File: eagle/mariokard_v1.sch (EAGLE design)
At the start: 64 parts, among them SW1 KMR2, SW2 KMR2, U1 SPX3819, U3 ATMEGA32U4, U4 L298, X1 ESP-12, Y1 16MHz

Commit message: small fixes - still WIP
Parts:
- added U$29: FTDI_POGO, digikey:FTDI_POGO
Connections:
- removed net D5: U3.PC6
- removed net D6: U3.PD7(ADC10)
- removed net DIRA: U4.IN1, U4.IN2
- removed net DIRB: U4.IN3, U4.IN4
- removed net PWMA: U4.ENA
- removed net PWMB: U4.ENB
- new net DIRA1: U4.IN1
- new net DIRA2: U4.IN2
- new net DIRB1: U4.IN3
- new net DIRB2: U4.IN4
- new net PWMA/D5: U3.PC6, U4.ENA
- new net PWMB/D6: U3.PD7(ADC10), U4.ENB
- net GND: now also U$29.GND
- net RXD_5V: now also U$29.TXD
- net TXD: now also U$29.RXD
- net VIN: now also U$29.VCC
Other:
- note added: "3.3 Logic Voltage"
- note added: "COLOR SENSOR"
- note added: "connect things to ATMega"
- note removed: "3.3 Reg Voltage"
- note removed: "accelerometer"
- moved on the sheet: CN1, CN2, D1, D2, D21, D22, D23, D24, D3, D4, D5, D6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

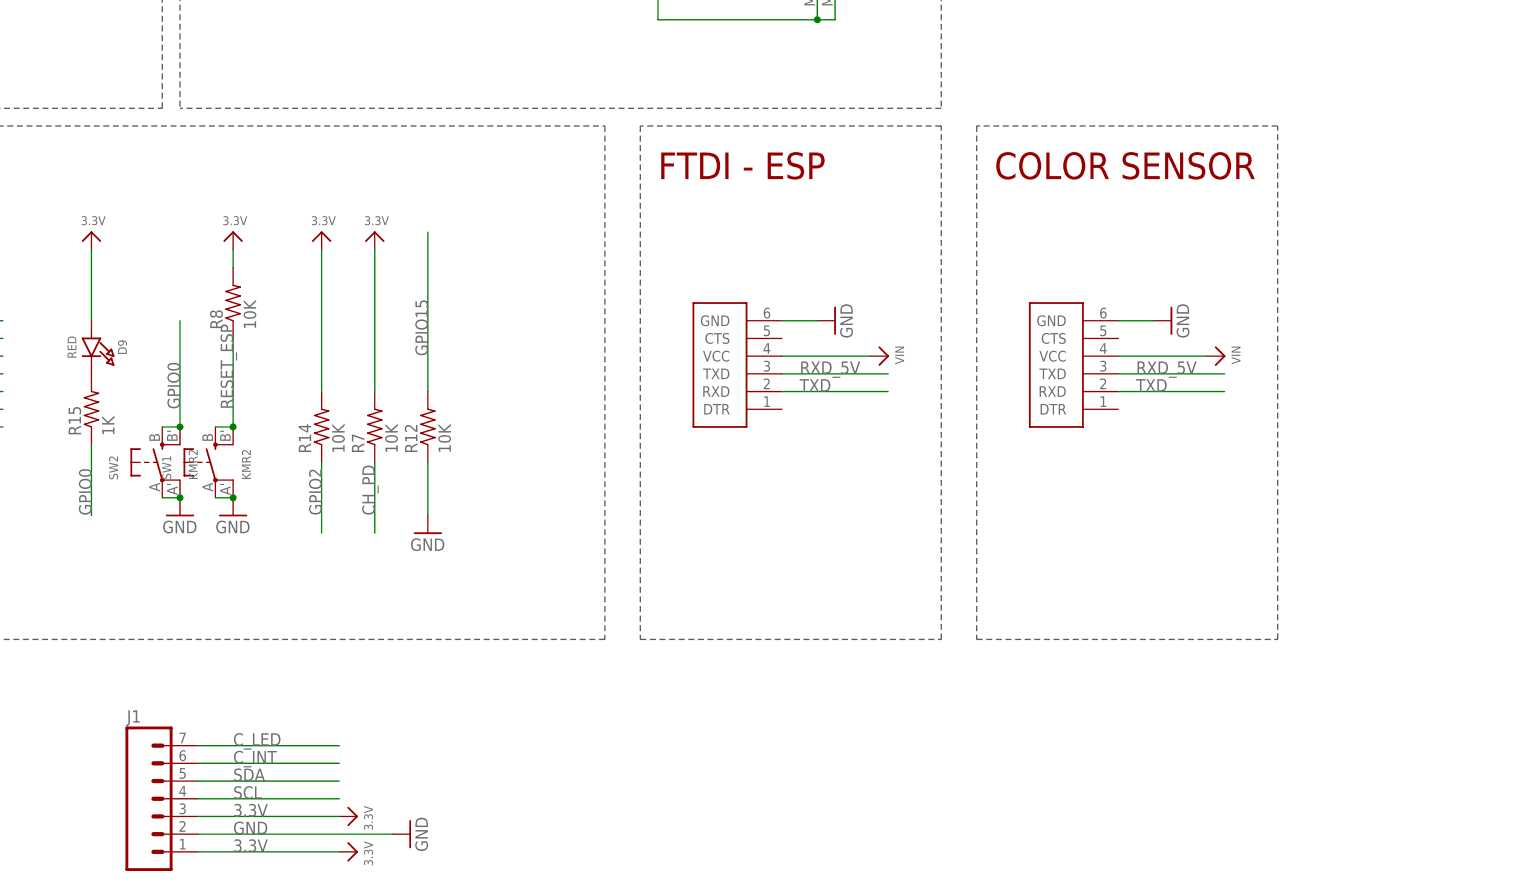
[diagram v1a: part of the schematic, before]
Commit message: fixed copy-paste error
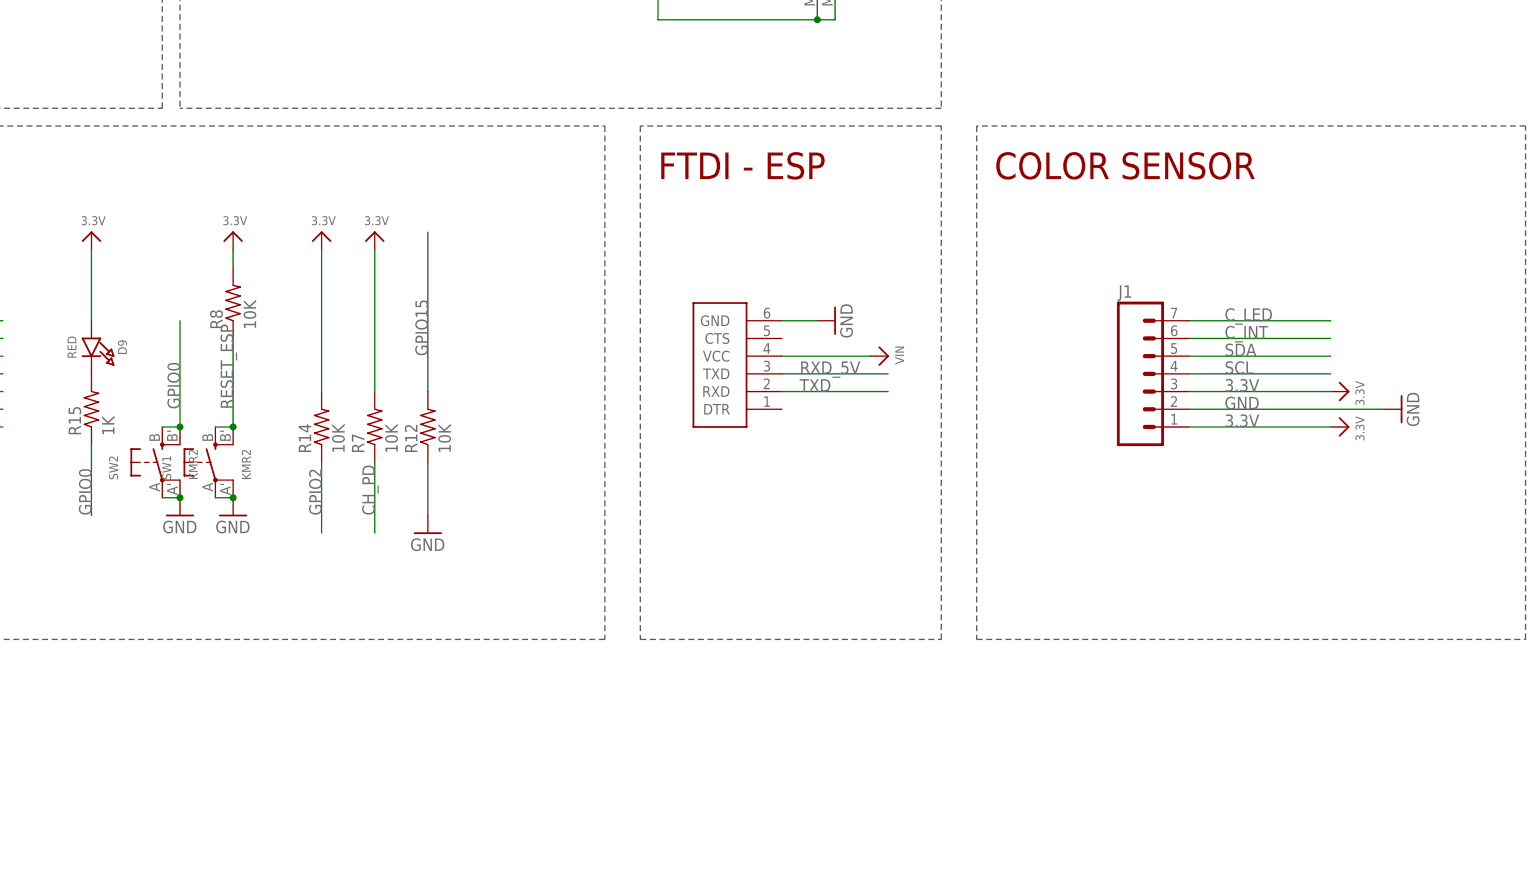
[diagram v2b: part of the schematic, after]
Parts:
- removed U$29: FTDI_POGO, digikey:FTDI_POGO
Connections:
- net GND: no longer U$29.GND
- net RXD_5V: no longer U$29.TXD
- net TXD: no longer U$29.RXD
- net VIN: no longer U$29.VCC
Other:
- moved on the sheet: J1
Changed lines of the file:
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@@
 <part name="GND15" library="supply1" deviceset="GND" device=""/>
 <part name="U$26" library="microbuilder" deviceset="3.3V" device=""/>
-<part name="U$29" library="digikey" deviceset="FTDI_POGO" device=""/>
-<part name="GND22" library="supply1" deviceset="GND" device=""/>
-<part name="U$35" library="microbuilder" deviceset="VIN" device=""/>
 </parts>
 <sheets>
@@
 <text x="22.86" y="-96.52" size="3.81" layer="94">Driver</text>
 <wire x1="411.48" y1="-35.56" x2="411.48" y2="-109.22" width="0.1524" layer="97" style="shortdash"/>
-<wire x1="411.48" y1="-109.22" x2="454.66" y2="-109.22" width="0.1524" layer="97" style="shortdash"/>
-<wire x1="454.66" y1="-109.22" x2="454.66" y2="-35.56" width="0.1524" layer="97" style="shortdash"/>
-<wire x1="454.66" y1="-35.56" x2="411.48" y2="-35.56" width="0.1524" layer="97" style="shortdash"/>
+<wire x1="411.48" y1="-109.22" x2="490.22" y2="-109.22" width="0.1524" layer="97" style="shortdash"/>
+<wire x1="490.22" y1="-109.22" x2="490.22" y2="-35.56" width="0.1524" layer="97" style="shortdash"/>
+<wire x1="490.22" y1="-35.56" x2="411.48" y2="-35.56" width="0.1524" layer="97" style="shortdash"/>
 <text x="414.02" y="-43.18" size="3.81" layer="94" ratio="10">COLOR SENSOR</text>
 <text x="-55.88" y="86.36" size="1.778" layer="97">connect things to ATMega</text>
@@
 <instance part="GND14" gate="1" x="241.3" y="60.96"/>
 <instance part="U$17" gate="G$1" x="165.1" y="86.36" rot="R90"/>
-<instance part="J1" gate="G$1" x="294.64" y="-134.62"/>
-<instance part="U$25" gate="G$1" x="322.58" y="-134.62" rot="R270"/>
-<instance part="GND15" gate="1" x="330.2" y="-137.16" rot="R90"/>
-<instance part="U$26" gate="G$1" x="322.58" y="-139.7" rot="R270"/>
-<instance part="U$29" gate="G$1" x="431.8" y="-63.5" rot="R180"/>
-<instance part="GND22" gate="1" x="439.42" y="-63.5" rot="R90"/>
-<instance part="U$35" gate="G$1" x="447.04" y="-68.58" rot="R270"/>
+<instance part="J1" gate="G$1" x="436.88" y="-73.66"/>
+<instance part="U$25" gate="G$1" x="464.82" y="-73.66" rot="R270"/>
+<instance part="GND15" gate="1" x="472.44" y="-76.2" rot="R90"/>
+<instance part="U$26" gate="G$1" x="464.82" y="-78.74" rot="R270"/>
 </instances>
 <busses>
@@
 <segment>
 <pinref part="J1" gate="G$1" pin="2"/>
-<wire x1="299.72" y1="-137.16" x2="327.66" y2="-137.16" width="0.1524" layer="91"/>
-<label x="304.8" y="-137.16" size="1.778" layer="95"/>
+<wire x1="441.96" y1="-76.2" x2="469.9" y2="-76.2" width="0.1524" layer="91"/>
+<label x="447.04" y="-76.2" size="1.778" layer="95"/>
 <pinref part="GND15" gate="1" pin="GND"/>
-</segment>
-<segment>
-<pinref part="U$29" gate="G$1" pin="GND"/>
-<pinref part="GND22" gate="1" pin="GND"/>
-<wire x1="431.8" y1="-63.5" x2="436.88" y2="-63.5" width="0.1524" layer="91"/>
 </segment>
 </net>
@@
 <pinref part="D23" gate="G$1" pin="C"/>
 </segment>
-<segment>
-<pinref part="U$29" gate="G$1" pin="VCC"/>
-<pinref part="U$35" gate="G$1" pin="VIN"/>
-<wire x1="431.8" y1="-68.58" x2="444.5" y2="-68.58" width="0.1524" layer="91"/>
-</segment>
 </net>
 <net name="RESET" class="0">
@@
 <segment>
 <pinref part="J1" gate="G$1" pin="3"/>
-<wire x1="299.72" y1="-134.62" x2="320.04" y2="-134.62" width="0.1524" layer="91"/>
-<label x="304.8" y="-134.62" size="1.778" layer="95"/>
+<wire x1="441.96" y1="-73.66" x2="462.28" y2="-73.66" width="0.1524" layer="91"/>
+<label x="447.04" y="-73.66" size="1.778" layer="95"/>
 <pinref part="U$25" gate="G$1" pin="3.3V"/>
 </segment>
 <segment>
 <pinref part="J1" gate="G$1" pin="1"/>
-<wire x1="299.72" y1="-139.7" x2="320.04" y2="-139.7" width="0.1524" layer="91"/>
-<label x="304.8" y="-139.7" size="1.778" layer="95"/>
+<wire x1="441.96" y1="-78.74" x2="462.28" y2="-78.74" width="0.1524" layer="91"/>
+<label x="447.04" y="-78.74" size="1.778" layer="95"/>
 <pinref part="U$26" gate="G$1" pin="3.3V"/>
 </segment>
@@
 <pinref part="U$19" gate="G$1" pin="RXD"/>
 </segment>
-<segment>
-<wire x1="447.04" y1="-73.66" x2="431.8" y2="-73.66" width="0.1524" layer="91"/>
-<label x="434.34" y="-73.66" size="1.778" layer="95"/>
-<pinref part="U$29" gate="G$1" pin="RXD"/>
-</segment>
 </net>
 <net name="RESET_5V" class="0">
@@
 <label x="386.08" y="-71.12" size="1.778" layer="95"/>
 <pinref part="U$19" gate="G$1" pin="TXD"/>
-</segment>
-<segment>
-<wire x1="447.04" y1="-71.12" x2="431.8" y2="-71.12" width="0.1524" layer="91"/>
-<label x="434.34" y="-71.12" size="1.778" layer="95"/>
-<pinref part="U$29" gate="G$1" pin="TXD"/>
 </segment>
 </net>
@@
 <segment>
 <pinref part="J1" gate="G$1" pin="7"/>
-<wire x1="299.72" y1="-124.46" x2="320.04" y2="-124.46" width="0.1524" layer="91"/>
-<label x="304.8" y="-124.46" size="1.778" layer="95"/>
+<wire x1="441.96" y1="-63.5" x2="462.28" y2="-63.5" width="0.1524" layer="91"/>
+<label x="447.04" y="-63.5" size="1.778" layer="95"/>
 </segment>
 </net>
@@
 <segment>
 <pinref part="J1" gate="G$1" pin="6"/>
-<wire x1="299.72" y1="-127" x2="320.04" y2="-127" width="0.1524" layer="91"/>
-<label x="304.8" y="-127" size="1.778" layer="95"/>
+<wire x1="441.96" y1="-66.04" x2="462.28" y2="-66.04" width="0.1524" layer="91"/>
+<label x="447.04" y="-66.04" size="1.778" layer="95"/>
 </segment>
 </net>
@@
 <segment>
 <pinref part="J1" gate="G$1" pin="5"/>
-<wire x1="299.72" y1="-129.54" x2="320.04" y2="-129.54" width="0.1524" layer="91"/>
-<label x="304.8" y="-129.54" size="1.778" layer="95"/>
+<wire x1="441.96" y1="-68.58" x2="462.28" y2="-68.58" width="0.1524" layer="91"/>
+<label x="447.04" y="-68.58" size="1.778" layer="95"/>
 </segment>
 <segment>
@@
 <segment>
 <pinref part="J1" gate="G$1" pin="4"/>
-<wire x1="299.72" y1="-132.08" x2="320.04" y2="-132.08" width="0.1524" layer="91"/>
-<label x="304.8" y="-132.08" size="1.778" layer="95"/>
-</segment>
-<segment>
+<wire x1="441.96" y1="-71.12" x2="462.28" y2="-71.12" width="0.1524" layer="91"/>
+<label x="447.04" y="-71.12" size="1.778" layer="95"/>
+</segment>
+<segment>

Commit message: v1 - still needs to be tested
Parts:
- removed CN1, CN2: (no value), adafruit:JST_2PIN-SMT-RA
- removed D1: 1n4148, microbuilder:DIODESOD-323
- removed SW1: KMR2, microbuilder:SWITCH_TACT_SMT4.6X2.8
- added MOTOR_LEFT, MOTOR_RIGHT: (no value), adafruit:JST_2PIN-SMT-RA
- added RESET: KMR2, microbuilder:SWITCH_TACT_SMT4.6X2.8
- renumbered D9 to GPIO0LED, J1 to COLOR_SENSOR, SW2 to GPIO0, U$11 to ISP, U$19 to FTDI
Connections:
- removed net C_INT: COLOR_SENSOR.6
- removed net C_LED: COLOR_SENSOR.7
- removed net D10: U3.PB6(ADC13)
- removed net D11: U3.PB7
- removed net D12: U3.PD6(ADC9)
- removed net D7: U3.PE6
- removed net D8: U3.PB4(ADC11)
- removed net D9: U3.PB5(ADC12)
- removed net DIRA1: U4.IN1
- removed net DIRA2: U4.IN2
- removed net DIRB1: U4.IN3
- removed net DIRB2: U4.IN4
- removed net N$24: COM.C
- removed net N$34: U$4.MTN1, U$4.MTN2, Z1.2, Z2.2
- removed net N$35: U$4.GND, U$4.MTN3, U$4.MTN4
- removed net RESET_5V: D1.C
- removed net RXI: U3.PD2(RX)
- removed net TXO: U3.PD3(TX)
- new net C_INT/D7: COLOR_SENSOR.6, U3.PE6
- new net C_LED/D8: COLOR_SENSOR.7, U3.PB4(ADC11)
- new net DIRA1/D9: U3.PB5(ADC12), U4.IN1
- new net DIRA2/D10: U3.PB6(ADC13), U4.IN2
- new net DIRB1/D11: U3.PB7, U4.IN3
- new net DIRB2/D12: U3.PD6(ADC9), U4.IN4
- net GND: now also COM.C, RESET.P, RESET.P1, U$4.GND, U$4.MTN1, U$4.MTN2, U$4.MTN3, U$4.MTN4, Z1.2, Z2.2; no longer SW1.P, SW1.P1
- net OUT1: now also MOTOR_RIGHT.2; no longer CN1.2
- net OUT2: now also MOTOR_RIGHT.1; no longer CN1.1
- net OUT3: now also MOTOR_LEFT.1; no longer CN2.1
- net OUT4: now also MOTOR_LEFT.2; no longer CN2.2
- net RESET_ESP: now also RESET.S, RESET.S1; no longer D1.A, SW1.S, SW1.S1
- net RXD: now also U3.PD2(RX), X1.TXD; no longer X1.RXD
- net TXD: now also U3.PD3(TX), X1.RXD; no longer X1.TXD
- net VBAT: now also D21.C, D23.C, D3.C, D5.C, U4.VS
- net VIN: no longer D21.C, D23.C, D3.C, D5.C, U4.VS
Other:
- note removed: "connect things to ATMega"
- moved on the sheet: R12, R14, R7, R8
